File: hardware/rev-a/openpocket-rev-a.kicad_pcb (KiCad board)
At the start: 8 copper layers, 115 x 72 mm, 315 parts, among them J1 ER-TFT050A3-2 FFC, J11 5.8 GHz antenna U.FL, J12 push-push microSD, J13 speaker solder pads, J14 SSD1306 128x64 OLED pads, J15 expander developer pads, J18 rotary encoder control pads, J19 ARM switch pads, J2 USB-C, J20 AUX2 three-position switch pa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, J21 AUX3 three-position switch pa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, J22 AUX4 three-position switch pa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, J23 AIL trim pads, J24 ELE trim pads, J25 THR trim pads, J26 RUD trim pads, J3 battery/NTC, J4 speaker connector, J5 master switch, J6 ELRS, J7 left gimbal, J8 right gimbal, J9 menu/UI control pads, Q1 dual protection FET, Q2 Q_BUZZ buzzer MOSFET, U1 ESP32-S3-MINI-1U-N8, U10 display 3V3 buck, U11 analog OSD, U12 OSD 3V3-to-5V, U13 OSD 5V-to-3V3, U14 CVBS TFT controller, U15 AMT boot flash, U16 AMT flash mux, U17 backlight boost, U18 GPIO expander 0x20, U19 GPIO expander 0x21, U2 1S charger/power path, U20 master load switch, U21 I2S speaker amplifier, U22 3V3_SD load switch, U3 1S protector, U4 fuel gauge, U5 3V3 buck-boost, U6 5V boost, U7 5V_VIDEO load switch, U8 5V_DISPLAY load switch, U9 5V_ELRS load switch, Y1 27.000MHz, Y2 27.000MHz

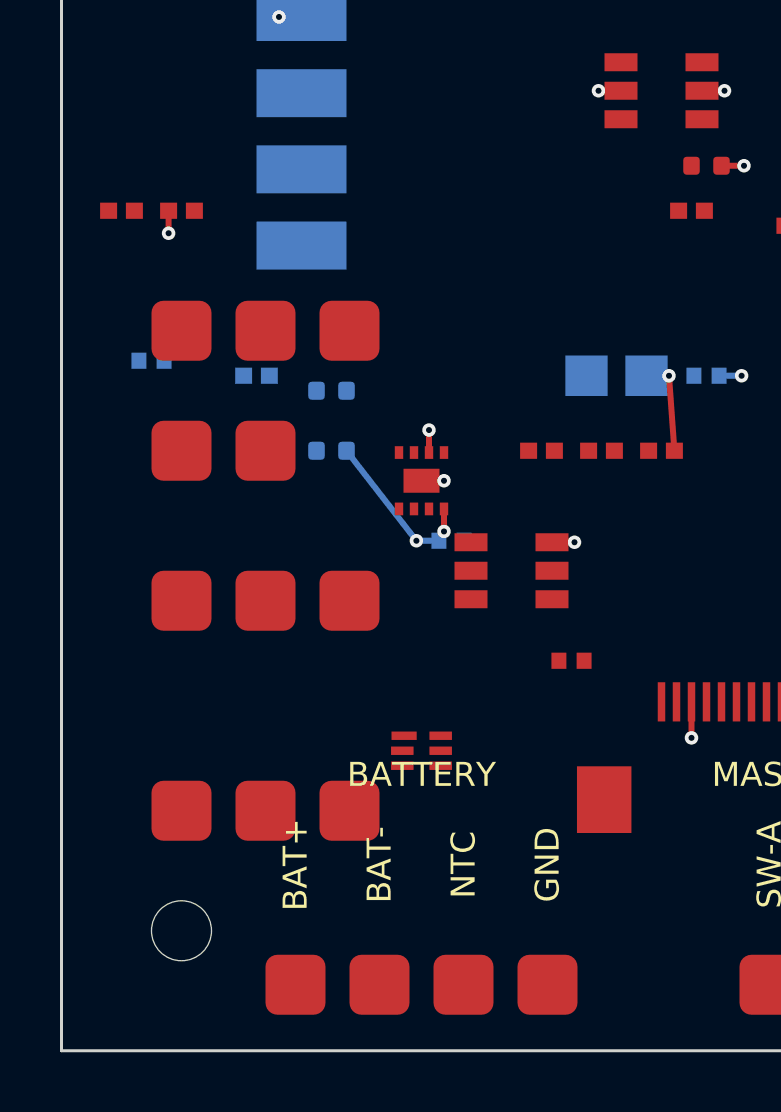
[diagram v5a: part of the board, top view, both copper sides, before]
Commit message: fix(rev-a): seed reviewed battery entry fanout
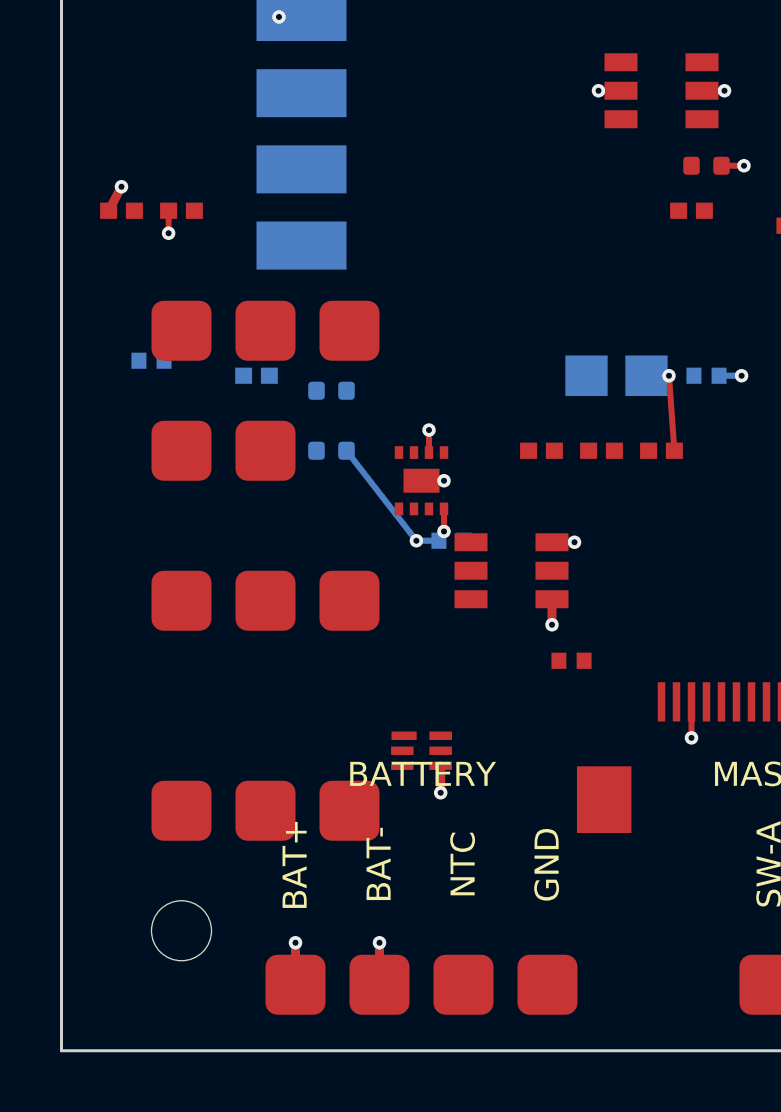
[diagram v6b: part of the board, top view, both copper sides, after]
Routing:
- net BAT_RAW: track 0.00 -> 33.3 mm, vias 0 -> 2
- net BAT_CELL_NEG: track 0.00 -> 16.1 mm, vias 0 -> 3
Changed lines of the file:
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@@
+	)
+	(segment
+		(start 12.64 63.4)
+		(end 12.64 62.5)
+		(width 0.3)
+		(layer "F.Cu")
+		(net 49)
+	)
+	(segment
+		(start 10.6 69.8)
+		(end 10.6 68.4)
+		(width 0.3)
+		(layer "F.Cu")
+		(net 49)
+	)
+	(segment
+		(start 16.35 57.8)
+		(end 16.35 56.95)
+		(width 0.3)
+		(layer "F.Cu")
+		(net 49)
+	)
+	(via
+		(at 12.64 63.4)
+		(size 0.45)
+		(drill 0.2)
+		(layers "F.Cu" "B.Cu")
+		(tenting front back)
+		(net 49)
+	)
+	(via
+		(at 10.6 68.4)
+		(size 0.45)
+		(drill 0.2)
+		(layers "F.Cu" "B.Cu")
+		(tenting front back)
+		(net 49)
+	)
+	(via
+		(at 16.35 57.8)
+		(size 0.45)
+		(drill 0.2)
+		(layers "F.Cu" "B.Cu")
+		(tenting front back)
+		(net 49)
+	)
+	(segment
+		(start 10.6 64.5)
+		(end 12.64 63.4)
+		(width 0.4)
+		(layer "In2.Cu")
+		(net 49)
+	)
+	(segment
+		(start 12.64 63.4)
+		(end 16.35 57.8)
+		(width 0.4)
+		(layer "In2.Cu")
+		(net 49)
+	)
+	(segment
+		(start 10.6 68.4)
+		(end 10.6 64.5)
+		(width 0.4)
+		(layer "In2.Cu")
+		(net 49)
+	)
+	(segment
+		(start 7.8 69.8)
+		(end 7.8 68.4)
+		(width 0.3)
+		(layer "F.Cu")
+		(net 53)
+	)
+	(segment
+		(start 2 43.2)
+		(end 1.57 44)
+		(width 0.3)
+		(layer "F.Cu")
+		(net 53)
+	)
+	(via
+		(at 7.8 68.4)
+		(size 0.45)
+		(drill 0.2)
+		(layers "F.Cu" "B.Cu")
+		(tenting front back)
+		(net 53)
+	)
+	(via
+		(at 2 43.2)
+		(size 0.45)
+		(drill 0.2)
+		(layers "F.Cu" "B.Cu")
+		(tenting front back)
+		(net 53)
+	)
+	(segment
+		(start 2 66.3)
+		(end 2 43.2)
+		(width 0.4)
+		(layer "In2.Cu")
+		(net 53)
+	)
+	(segment
+		(start 7.8 68.4)
+		(end 7.8 66.3)
+		(width 0.4)
+		(layer "In2.Cu")
+		(net 53)
+	)
+	(segment
+		(start 7.8 66.3)
+		(end 2 66.3)
+		(width 0.4)
+		(layer "In2.Cu")
+		(net 53)
 	)
 	(segment

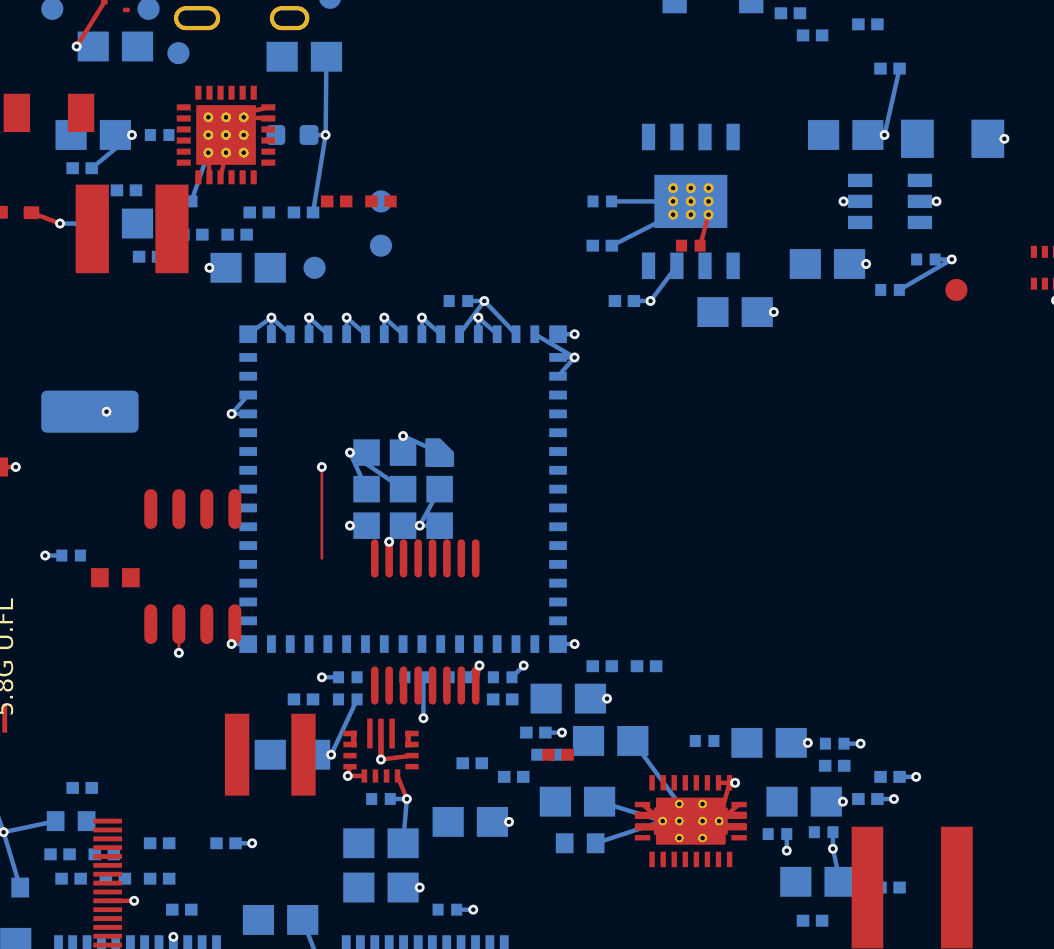
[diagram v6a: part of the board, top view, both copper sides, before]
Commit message: fix(rev-a): reserve ESP32 backside fanout corridor
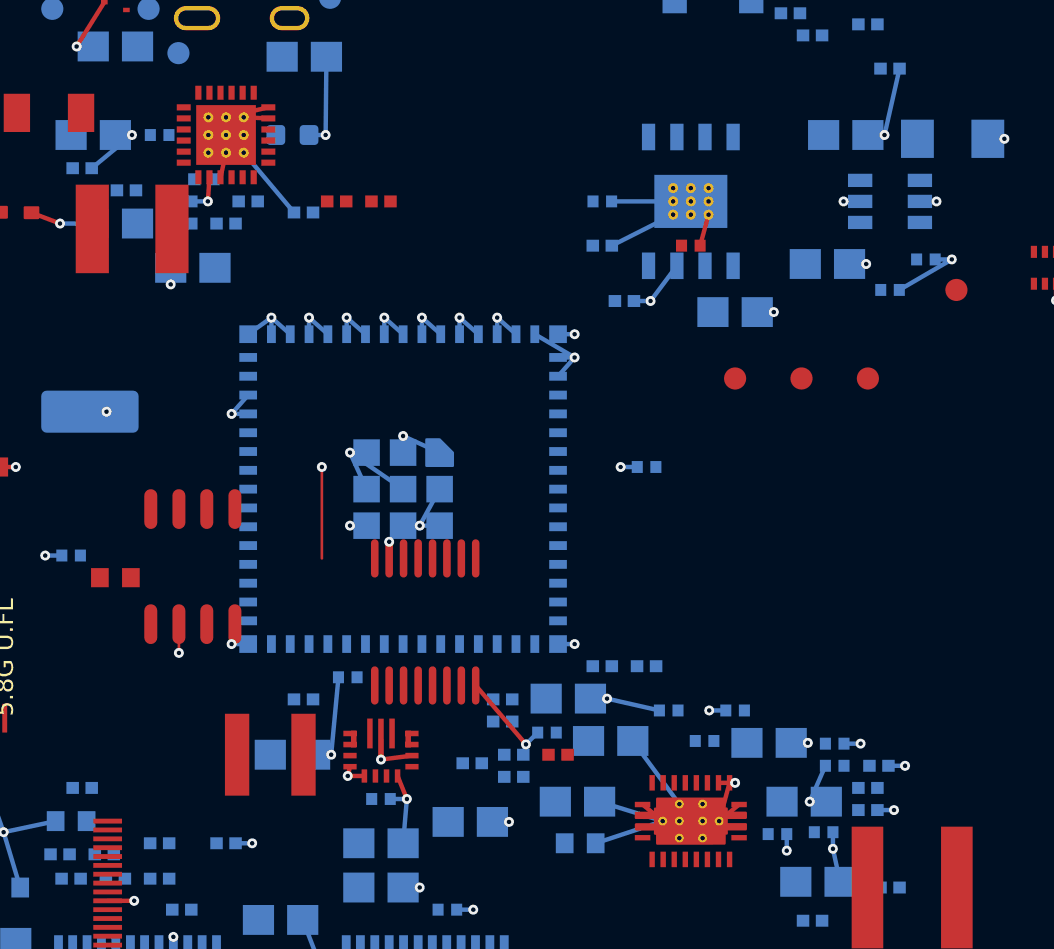
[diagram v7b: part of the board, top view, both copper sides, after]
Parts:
- TP44, TP45, TP46: moved to F.Cu
- moved TP46 22.8 mm to (86.0, 26.0)
- moved TP45 20.6 mm to (83.0, 26.0)
- moved TP44 19.6 mm to (80.0, 26.0)
- moved C81 15.5 mm to (84.5, 43.5), turned to 180 degrees
- moved C79 14.6 mm to (80.0, 41.0), turned to 180 degrees
- moved C1 11.3 mm to (76.0, 30.0), turned to 180 degrees
- moved C80 9.62 mm to (77.0, 41.0), turned to 180 degrees
- moved C78 9.12 mm to (71.5, 42.0), turned to 180 degrees
- moved R49 3.20 mm to (69.5, 40.5)
- moved R45 2.92 mm to (56.0, 17.0), turned to 180 degrees
- moved C32 2.50 mm to (55.5, 21.0)
- moved R43 2.12 mm to (55.0, 19.0)
- moved R20 1.80 mm to (86.0, 44.5)
- moved R44 1.58 mm to (57.0, 19.0)
- moved R23 1.41 mm to (70.0, 43.0)
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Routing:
- net GND: track 259.4 -> 260.4 mm, vias 145 -> 144

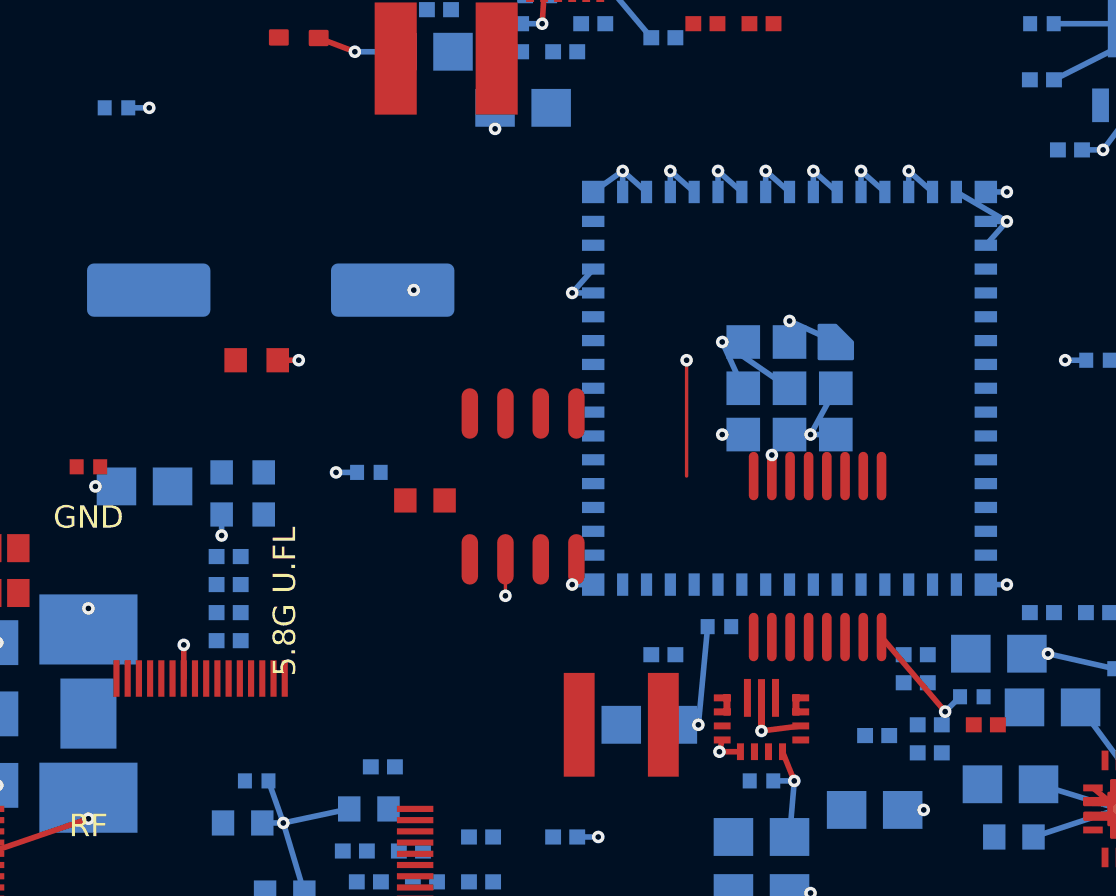
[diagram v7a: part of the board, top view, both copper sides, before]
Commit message: fix(rev-a): clear AMT mux from ESP32 underside
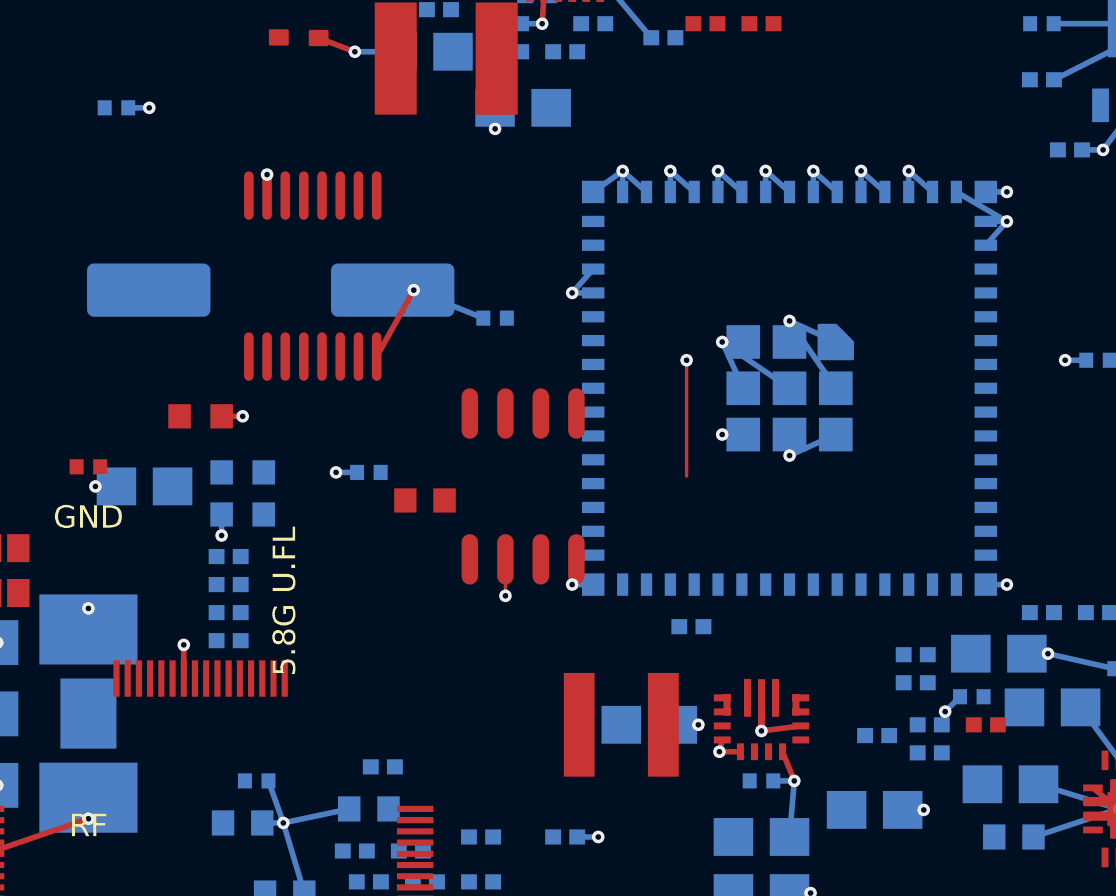
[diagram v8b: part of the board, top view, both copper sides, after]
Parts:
- moved U16 20.6 mm to (48.0, 27.0)
- moved C71 13.6 mm to (54.5, 28.5)
- moved R103 2.83 mm to (44.0, 32.0)
- moved R95 1.41 mm to (61.5, 39.5)
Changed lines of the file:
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@@
 	(footprint "R0603"
 		(layer "F.Cu")
-		(at 46 30)
+		(at 44 32)
 		(property "Reference" "R103"
 			(at 0 -4 0)
@@
 	(footprint "TSSOP-16_L5.0-W4.4-P0.65-LS6.4-BL"
 		(layer "F.Cu")
-		(at 66 37)
+		(at 48 27)
 		(property "Reference" "U16"
 			(at 0 -6.866 0)
@@
 	(footprint "C0402"
 		(layer "B.Cu")
-		(at 62.5 39.5 180)
+		(at 54.5 28.5 180)
 		(descr "22nF (223) ±10% 50V")
 		(property "Reference" "C71"
@@
 	(footprint "R0402"
 		(layer "B.Cu")
-		(at 60.5 40.5)
+		(at 61.5 39.5)
 		(property "Reference" "R95"
 			(at 0 4 0)
@@
 	)
 	(segment
-		(start 68.28 39.87)
-		(end 70.549669 42.53033)
+		(start 50.28 29.87)
+		(end 51.6 27.5)
 		(width 0.2)
 		(layer "F.Cu")
@@
 	)
 	(segment
-		(start 64.37 34.13)
-		(end 64.37 33.38)
+		(start 46.37 24.13)
+		(end 46.37 23.38)
 		(width 0.2)
 		(layer "F.Cu")
@@
 	)
 	(segment
-		(start 46.75 30)
-		(end 47.5 30)
+		(start 44.75 32)
+		(end 45.5 32)
 		(width 0.2)
 		(layer "F.Cu")
@@
 	)
 	(via
-		(at 47.5 30)
+		(at 45.5 32)
 		(size 0.45)
 		(drill 0.2)
@@
 	)
 	(via
-		(at 65.75 32.65)
+		(at 65 33.4)
 		(size 0.45)
 		(drill 0.2)
@@
 	)
 	(via
-		(at 64.37 33.38)
+		(at 46.37 23.38)
 		(size 0.45)
 		(drill 0.2)
@@
 	(segment
 		(start 65 32.65)
-		(end 65.75 32.65)
+		(end 65 33.4)
 		(width 0.2)
 		(layer "B.Cu")
@@
 	)
 	(segment
-		(start 62.08 39.5)
-		(end 61.75 43)
+		(start 54.08 28.5)
+		(end 51.6 27.5)
 		(width 0.2)
 		(layer "B.Cu")
@@
 	(segment
 		(start 66.65 32.65)
-		(end 65.75 32.65)
+		(end 65 33.4)
 		(width 0.2)
 		(layer "B.Cu")
@@
 	(segment
 		(start 66.65 31)
-		(end 65.75 32.65)
+		(end 65 28.6)
 		(width 0.2)
 		(layer "B.Cu")
